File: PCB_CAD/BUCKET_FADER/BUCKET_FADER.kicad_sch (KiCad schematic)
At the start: 62 parts, among them J1 POW, J2 MOTOR, J3 POS_TOUCH, J4 F0_BTN, J5 F1_BTN, J6 F2_BTN, J7 F3_BTN, J8 AUDIO_METER, U1 AT42QT1011-M, U2 AT42QT1011-M, U3 AT42QT1011-M, U4 AT42QT1011-M, U5 DRV8871DDA, U6 DRV8871DDA, U7 DRV8871DDA, U8 DRV8871DDA

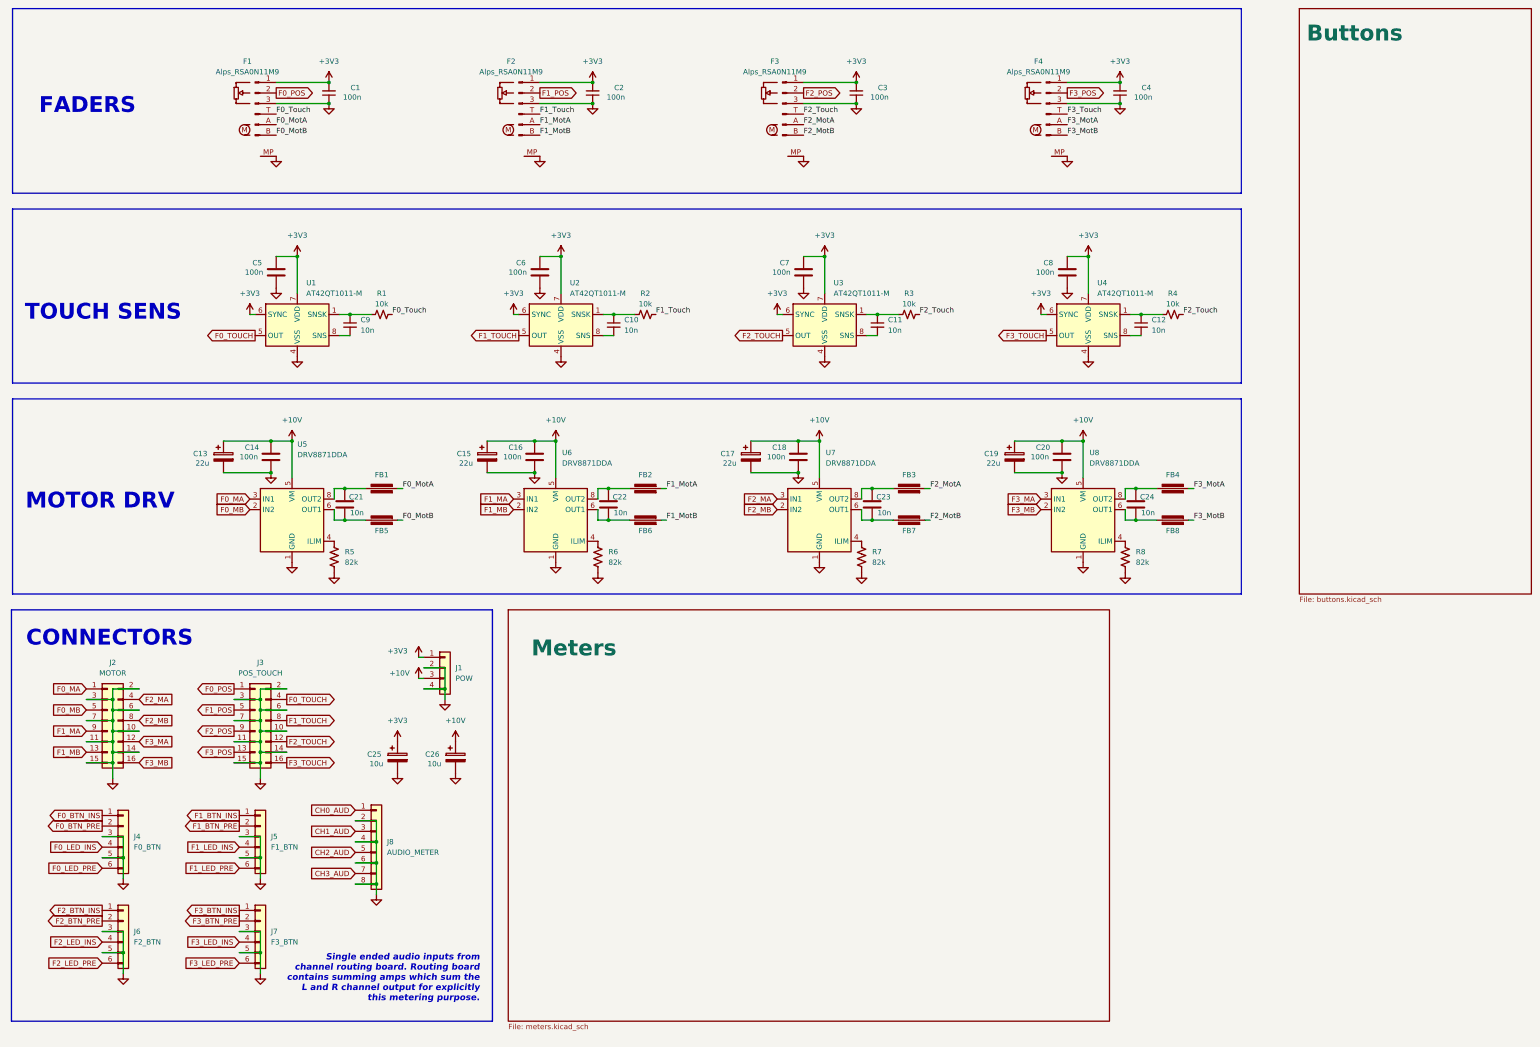
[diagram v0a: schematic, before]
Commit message: fader board design done
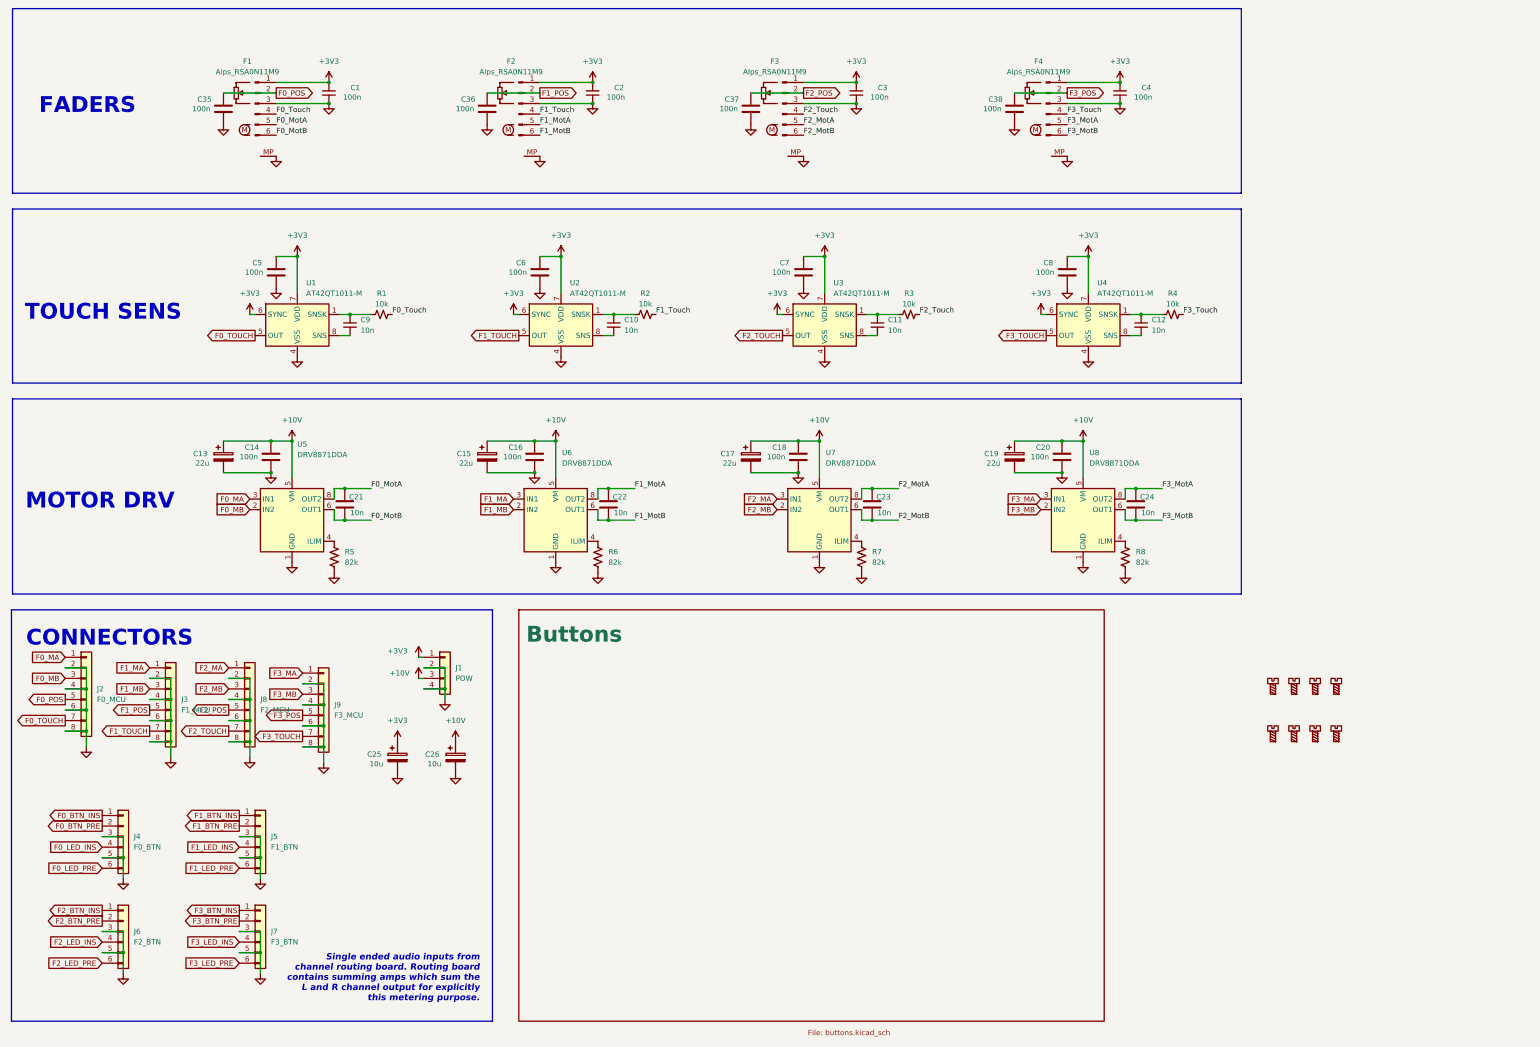
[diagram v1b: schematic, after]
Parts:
- removed FB1, FB2, FB3, FB4, FB5, FB6, FB7, FB8: FerriteBead, PCM_Ferrite_SMD_AKL:Ferrite_0603_1608Metric, symbol PCM_Device_AKL:Ferrite_Bead
- removed J2: MOTOR, symbol Connector_Generic:Conn_02x08_Odd_Even
- removed J3: POS_TOUCH, symbol Connector_Generic:Conn_02x08_Odd_Even
- added C35, C36, C37, C38: 100n, Capacitor_SMD:C_0402_1005Metric, symbol Device:C
- added H1, H2, H3, H4, H5, H6, H7, H8: MountingScrew, MountingHole:MountingHole_2.2mm_M2, symbol Auxiliary_Items:MountingScrew
- added J2: F0_MCU, Connector_PinHeader_2.54mm:PinHeader_1x08_P2.54mm_Vertical, symbol Connector_Generic:Conn_01x08
- added J3: F1_MCU, Connector_PinHeader_2.54mm:PinHeader_1x08_P2.54mm_Vertical, symbol Connector_Generic:Conn_01x08
- added J9: F3_MCU, Connector_PinHeader_2.54mm:PinHeader_1x08_P2.54mm_Vertical, symbol Connector_Generic:Conn_01x08
- C1, C14, C16, C18, C2, C20, C3, C4, C5, C6, C7, C8: footprint PCM_Capacitor_SMD_AKL:C_0603_1608Metric -> Capacitor_SMD:C_0402_1005Metric; LCSC C1591 -> C1525
- C10, C11, C12, C21, C22, C23, C24, C9: footprint (none) -> Capacitor_SMD:C_0402_1005Metric; LCSC (none) -> C1524
- C13, C15, C17, C19: footprint PCM_Capacitor_SMD_AKL:C_0603_1608Metric -> Capacitor_SMD:CP_Elec_5x5.4; LCSC C1591 -> C15848
- C25, C26: footprint PCM_Capacitor_SMD_AKL:C_0603_1608Metric -> Capacitor_SMD:C_1206_3216Metric; LCSC C1591 -> C1849
- F1, F2, F3, F4: footprint My Footprints:Alps RSA0N11M9 DEV -> Connector_PinHeader_2.54mm:PinHeader_1x06_P2.54mm_Vertical; LCSC (none) -> dnp
- J1: footprint 4ms_Connector:Pins_1x04_2.54mm_TH_SWD -> Connector_PinHeader_2.54mm:PinHeader_1x04_P2.54mm_Vertical; LCSC (none) -> dnp
- J4, J5, J6, J7: footprint (none) -> Connector_PinHeader_2.54mm:PinHeader_1x06_P2.54mm_Vertical; LCSC (none) -> dnp
- J8: value AUDIO_METER -> F2_MCU; footprint (none) -> Connector_PinHeader_2.54mm:PinHeader_1x08_P2.54mm_Vertical; LCSC (none) -> dnp
- R1, R2, R3, R4: footprint (none) -> Resistor_SMD:R_0603_1608Metric; LCSC (none) -> C15401
- R5, R6, R7, R8: footprint (none) -> Resistor_SMD:R_0603_1608Metric; LCSC (none) -> C1275
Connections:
- net CH0_AUD is gone; now on net F2_MA: J8.1 (Pin_1)
- net CH1_AUD is gone; now on net F2_MB: J8.3 (Pin_3)
- net CH2_AUD is gone; now on net F2_POS: J8.5 (Pin_5)
- net CH3_AUD is gone; now on net F2_TOUCH: J8.7 (Pin_7)
- net F0_MA: now also J2.1 (Pin_1)
- net F0_MB: now also J2.3 (Pin_3)
- net F0_MotA: now also C21.1, F1.5 (A), U5.8 (OUT2); no longer F1.A (Pin_5)
- net F0_MotB: now also C21.2, F1.6 (B), U5.6 (OUT1); no longer F1.B (Pin_6)
- net F0_POS: now also C35.2, J2.5 (Pin_5)
- net F0_TOUCH: now also J2.7 (Pin_7)
- net F0_Touch: now also F1.4 (T); no longer F1.T (Pin_4)
- net F1_MA: now also J3.1 (Pin_1)
- net F1_MB: now also J3.3 (Pin_3)
- net F1_MotA: now also C22.1, F2.5 (A), U6.8 (OUT2); no longer F2.A (Pin_5)
- net F1_MotB: now also C22.2, F2.6 (B), U6.6 (OUT1); no longer F2.B (Pin_6)
- net F1_POS: now also C36.2, J3.5 (Pin_5)
- net F1_TOUCH: now also J3.7 (Pin_7)
- net F1_Touch: now also F2.4 (T); no longer F2.T (Pin_4)
- net F2_MotA: now also C23.1, F3.5 (A), U7.8 (OUT2); no longer F3.A (Pin_5)
- net F2_MotB: now also C23.2, F3.6 (B), U7.6 (OUT1); no longer F3.B (Pin_6)
- net F2_POS: now also C37.2
- net F2_Touch: now also F3.4 (T); no longer F3.T (Pin_4), R4.2
- net F3_MA: now also J9.1 (Pin_1)
- net F3_MB: now also J9.3 (Pin_3)
- net F3_MotA: now also C24.1, F4.5 (A), U8.8 (OUT2); no longer F4.A (Pin_5)
- net F3_MotB: now also C24.2, F4.6 (B), U8.6 (OUT1); no longer F4.B (Pin_6)
- net F3_POS: now also C38.2, J9.5 (Pin_5)
- net F3_TOUCH: now also J9.7 (Pin_7)
- net F3_Touch: now also F4.4 (T), R4.2; no longer F4.T (Pin_4)
- net GND: now also C35.1, C36.1, C37.1, C38.1, J2.2 (Pin_2), J2.4 (Pin_4), J2.6 (Pin_6), J2.8 (Pin_8), J3.2 (Pin_2), J3.4 (Pin_4), J3.6 (Pin_6), J3.8 (Pin_8), J9.2 (Pin_2), J9.4 (Pin_4), J9.6 (Pin_6), J9.8 (Pin_8)
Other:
- removed sheet Meters
